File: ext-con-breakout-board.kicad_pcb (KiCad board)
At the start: 4 copper layers, 46 x 33.1 mm, 9 parts, among them J1 Conn_02x12_Odd_Even, J2 Conn_01x16

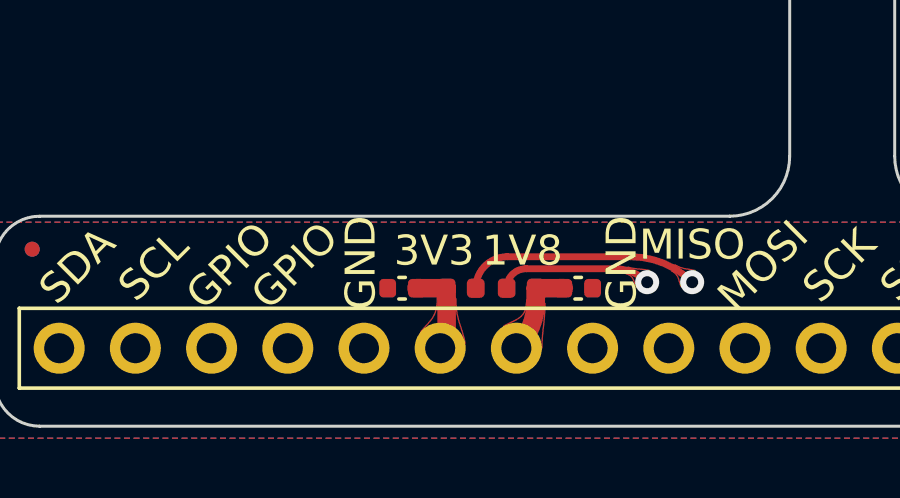
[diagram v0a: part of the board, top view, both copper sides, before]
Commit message: Add teardrops to the 0402 pads, add GND trace from C2 to the through hole pin, make the FPC connector part number be Panasonic AXT624124, add a 3D model for the FPC connector, fix and wave all DRCs on KiCad version 7.0.1, and update the board to be v0.7
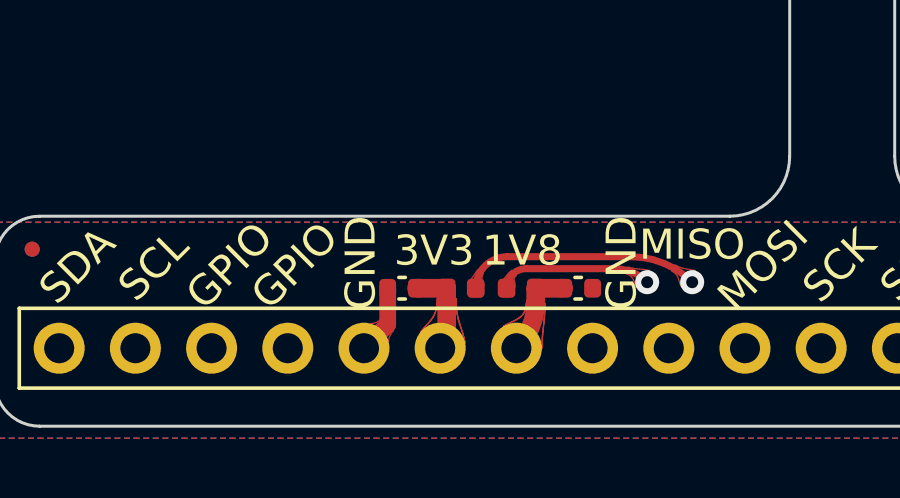
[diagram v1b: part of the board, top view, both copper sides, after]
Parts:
- J1: footprint ext-con-breakout-board:OK-06M024-04 -> ext-con-breakout-board:AXT624124
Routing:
- net GND: track 8.88 -> 11.2 mm
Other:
- board text added: "EXT CON Breakout Board v0.7"
- board text removed: "EXT CON Breakout Board v0.6"

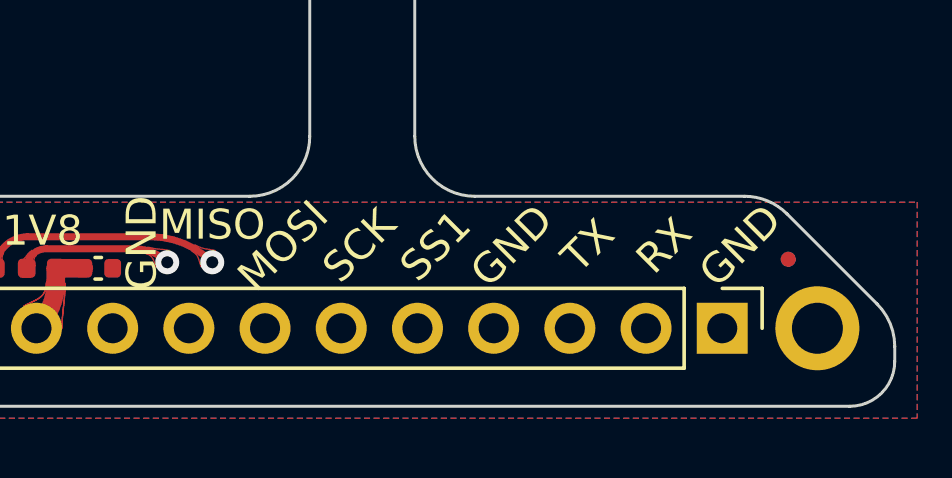
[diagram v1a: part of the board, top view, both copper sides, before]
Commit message: Add a silkscreen arrow pointing at the MISO pin
Add a third fiducial. Reduce the thermal relief gap to 0.428mm so that
the GND pins can have four spokes connecting to the copper pour on
ln2.Cu.

Fix the hatched lines drawn in the "Flex Section" on the User.Comments
layer.
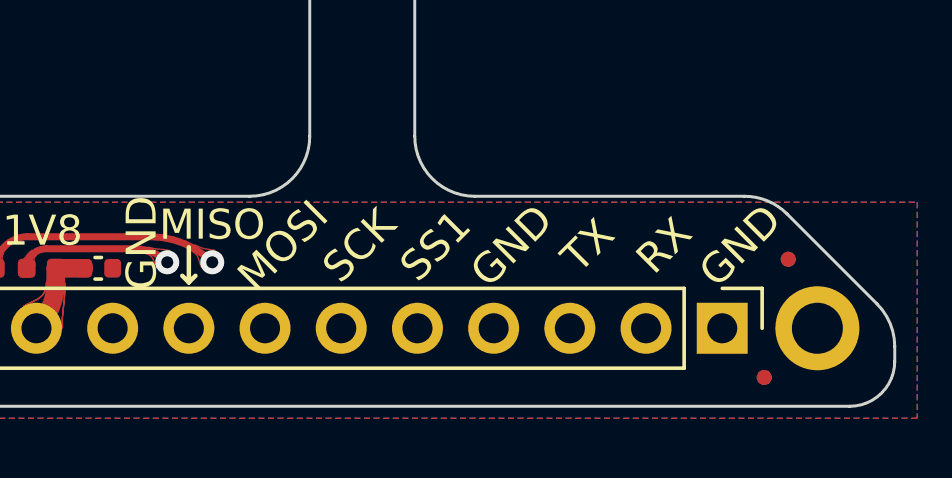
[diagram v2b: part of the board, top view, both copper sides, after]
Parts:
- added FID3: Fiducial, ext-con-breakout-board:Fiducial_0.5mm_Mask1mm, F.Cu at (131.9, 117.1)
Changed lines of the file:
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@@
   (net 22 "unconnected-(J1-Pin_20-Pad20)")
   (net 23 "unconnected-(J1-Pin_24-Pad24)")
+  (footprint "ext-con-breakout-board:Fiducial_0.5mm_Mask1mm" (layer "F.Cu")
+    (at 131.9 117.14)
+    (descr "Circular Fiducial, 0.5mm bare copper, 1mm soldermask opening (Level C)")
+    (tags "fiducial")
+    (property "Sheetfile" "ext-con-breakout-board.kicad_sch")
+    (property "Sheetname" "")
+    (property "ki_description" "Fiducial Marker")
+    (property "ki_keywords" "fiducial marker")
+    (attr smd)
+    (fp_text reference "FID3" (at 0 -1.5) (layer "F.SilkS") hide
+        (effects (font (size 1 1) (thickness 0.15)))
+    )
+    (fp_text value "Fiducial" (at 0 1.5) (layer "F.Fab") hide
+        (effects (font (size 1 1) (thickness 0.15)))
+    )
+    (fp_text user "${REFERENCE}" (at 0 0) (layer "F.Fab")
+        (effects (font (size 0.2 0.2) (thickness 0.04)))
+    )
+    (fp_circle (center 0 0) (end 0.75 0)
+      (stroke (width 0.05) (type solid)) (fill none) (layer "F.CrtYd"))
+    (fp_circle (center 0 0) (end 0.5 0)
+      (stroke (width 0.1) (type solid)) (fill none) (layer "F.Fab"))
+    (pad "" smd circle (at 0 0) (size 0.5 0.5) (layers "F.Cu" "F.Mask")
+      (solder_mask_margin 0.25) (clearance 0.25))
+    (pad "" smd circle (at 0 0) (size 0.5 0.5) (layers "B.Cu" "B.Mask")
+      (solder_mask_margin 0.25) (clearance 0.25))
+  )
   (footprint "Inductor_SMD:L_0402_1005Metric" (layer "F.Cu")
     (at 105.8 113.5 180)
@@
     (property "ki_description" "Mounting Hole with connection")
     (property "ki_keywords" "mounting hole")
-    (attr exclude_from_pos_files exclude_from_bom)
+    (attr exclude_from_pos_files)
     (fp_text reference "H1" (at 0 -3) (layer "F.SilkS") hide
         (effects (font (size 1 1) (thickness 0.15)))
@@
       (solder_mask_margin 0.25) (clearance 0.25))
   )
+  (gr_line (start 112.72 113.97) (end 112.94 113.75)
+    (stroke (width 0.15) (type default)) (layer "F.SilkS"))
+  (gr_line (start 112.72 113.97) (end 112.5 113.75)
+    (stroke (width 0.15) (type default)) (layer "F.SilkS"))
+  (gr_line (start 112.72 112.8) (end 112.72 113.97)
+    (stroke (width 0.15) (type default)) (layer "F.SilkS"))
   (gr_arc (start 122.95 85.65) (mid 122.575621 86.12207) (end 122 86.3)
     (stroke (width 0.1) (type solid)) (layer "Cmts.User"))
@@
   (gr_arc (start 90.25 112.6) (mid 90.68934 111.53934) (end 91.75 111.1)
     (stroke (width 0.25) (type solid)) (layer "Cmts.User"))
-  (gr_line (start 116.75 106.1) (end 120.3 109.65)
+  (gr_line (start 116.75 106.2) (end 120.39 109.83)
     (stroke (width 0.1) (type solid)) (layer "Cmts.User"))
   (gr_line (start 117.45 88.7) (end 120.25 91.5)
     (stroke (width 0.1) (type solid)) (layer "Cmts.User"))
   (gr_arc (start 116.75 109.1) (mid 116.164214 110.514214) (end 114.75 111.1)
-    (stroke (width 0.1) (type solid)) (layer "Cmts.User"))
-  (gr_line (start 116.75 105.1) (end 120.25 108.6)
     (stroke (width 0.1) (type solid)) (layer "Cmts.User"))
   (gr_arc (start 132.2 90) (mid 131.907107 90.707107) (end 131.2 91)
@@
   (gr_line (start 123.9 91) (end 131.2 91)
     (stroke (width 0.15) (type solid)) (layer "Cmts.User"))
-  (gr_line (start 116.75 104.6) (end 120.25 108.1)
+  (gr_line (start 116.75 105.1) (end 120.25 108.6)
     (stroke (width 0.1) (type solid)) (layer "Cmts.User"))
   (gr_arc (start 117.534221 88.515701) (mid 118.954051 86.895969) (end 121.0239 86.3)
     (stroke (width 0.1) (type solid)) (layer "Cmts.User"))
-  (gr_line (start 120.25 91.16) (end 120.25 112.6)
+  (gr_line (start 120.25 91.16) (end 120.25 109.1)
     (stroke (width 0.1) (type solid)) (layer "Cmts.User"))
   (gr_arc (start 122.25 111.1) (mid 120.835786 110.514214) (end 120.25 109.1)
     (stroke (width 0.1) (type solid)) (layer "Cmts.User"))
-  (gr_line (start 116.75 103.1) (end 120.25 106.6)
+  (gr_line (start 116.75 103.9) (end 120.25 107.4)
     (stroke (width 0.1) (type solid)) (layer "Cmts.User"))
   (gr_line (start 117.209859 89.184682) (end 117.534221 88.515701)
@@
     (effects (font (size 1.5 1.5) (thickness 0.3)))
   )
-  (gr_text "Flex Section" (at 118.5 100.5 90) (layer "Cmts.User")
+  (gr_text "Flex Section" (at 118.5 100.25 90) (layer "Cmts.User")
     (effects (font (size 1 1) (thickness 0.2)))
   )
@@
   )
   (dimension (type aligned) (layer "Cmts.User")
-    (pts (xy 90.25 116.6) (xy 136.25 116.6))
+    (pts (xy 90.2 116.56) (xy 136.2 116.56))
     (height 5.4)
-    (gr_text "46.0000 mm" (at 113.25 120.2) (layer "Cmts.User")
+    (gr_text "46.0000 mm" (at 113.2 120.16) (layer "Cmts.User")
       (effects (font (size 1.5 1.5) (thickness 0.3)))
     )
@@
   )
   (dimension (type orthogonal) (layer "Cmts.User")
-    (pts (xy 134.75 118.1) (xy 131.242572 111.1))
+    (pts (xy 134.7 118.06) (xy 131.192572 111.06))
     (height 3.25)
     (orientation 1)
-    (gr_text "7.0000 mm" (at 140 114.6 90) (layer "Cmts.User")
+    (gr_text "7.0000 mm" (at 139.95 114.56 90) (layer "Cmts.User")
       (effects (font (size 1.5 1.5) (thickness 0.3)))
     )
@@
     (connect_pads (clearance 0.17))
     (min_thickness 0.23) (filled_areas_thickness no)
-    (fill yes (thermal_gap 0.508) (thermal_bridge_width 0.508))
+    (fill yes (thermal_gap 0.428) (thermal_bridge_width 0.508))
     (polygon
       (pts
@@
     (connect_pads (clearance 0.17))
     (min_thickness 0.23) (filled_areas_thickness no)
-    (fill yes (thermal_gap 0.508) (thermal_bridge_width 0.508))
-    (polygon
-      (pts
+    (fill yes (thermal_gap 0.4) (thermal_bridge_width 0.508))
+    (polygon
+      (pts
